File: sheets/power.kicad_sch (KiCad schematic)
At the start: 85 parts, among them Q11 C1815, Q12 A1015, Q13 A1442, T1 COIL, U11 74LS05, U12 74LS06, U28 PC4741, U29 PC4741, U33 74AS04, U37 LM2576T-5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

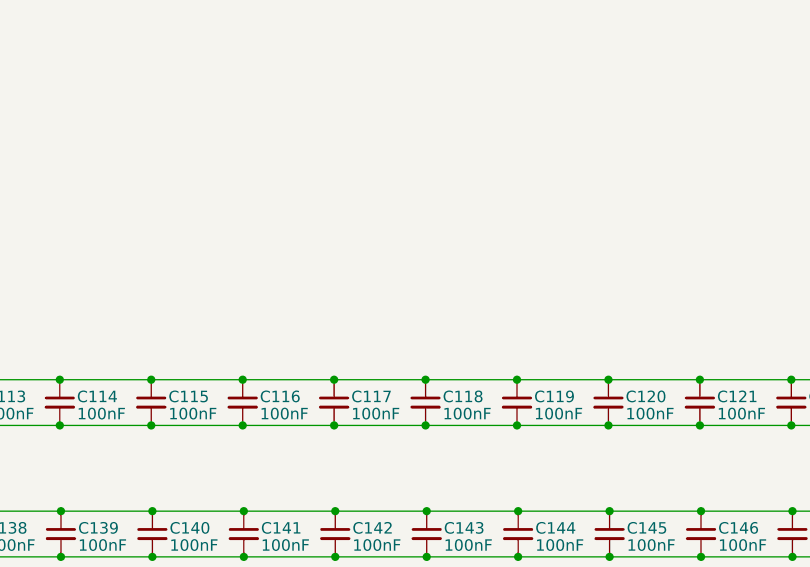
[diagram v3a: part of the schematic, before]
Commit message: Added LED
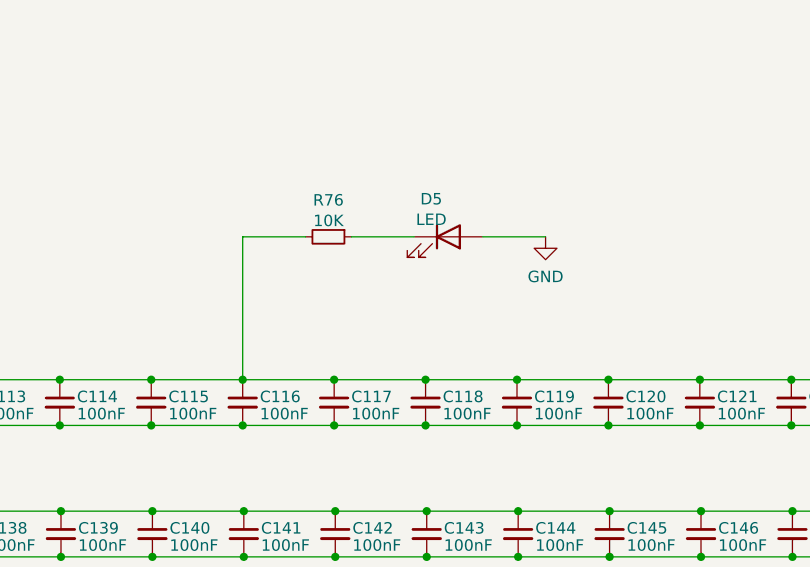
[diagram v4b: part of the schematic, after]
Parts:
- added D5: LED, 1_NeoGeoLibrary:Resistor1-5mm, symbol Device:LED
- added R76: 10K, Resistor_THT:R_Axial_DIN0309_L9.0mm_D3.2mm_P25.40mm_Horizontal, symbol Device:R_Small
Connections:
- net GND: now also D5.2 (A)
- net VCC: now also R76.2
- new net: D5.1 (K), R76.1
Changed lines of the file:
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@@
+    (stroke (width 0) (type default) (color 0 0 0 0))
+  )
+  (wire (pts (xy 197.485 111.125) (xy 204.47 111.125))
     (stroke (width 0) (type default) (color 0 0 0 0))
   )
@@
     (stroke (width 0) (type default) (color 0 0 0 0))
   )
+  (wire (pts (xy 170.815 127) (xy 170.815 111.125))
+    (stroke (width 0) (type default) (color 0 0 0 0))
+  )
   (wire (pts (xy 28.575 127) (xy 38.735 127))
     (stroke (width 0) (type default) (color 0 0 0 0))
@@
     (stroke (width 0) (type default) (color 0 0 0 0))
   )
+  (wire (pts (xy 170.815 111.125) (xy 177.8 111.125))
+    (stroke (width 0) (type default) (color 0 0 0 0))
+  )
   (wire (pts (xy 89.662 141.605) (xy 99.822 141.605))
     (stroke (width 0) (type default) (color 0 0 0 0))
@@
   )
   (wire (pts (xy 22.86 218.44) (xy 22.86 223.52))
+    (stroke (width 0) (type default) (color 0 0 0 0))
+  )
+  (wire (pts (xy 182.88 111.125) (xy 189.865 111.125))
     (stroke (width 0) (type default) (color 0 0 0 0))
   )
@@
     (pin "2")
   )
+  (symbol (lib_id "Device:R_Small") (at 180.34 111.125 270) (unit 1)
+    (in_bom yes) (on_board yes)
+    (property "Reference" "R76" (id 0) (at 180.34 107.061 90))
+    (property "Value" "10K" (id 1) (at 180.34 109.347 90))
+    (property "Footprint" "Resistor_THT:R_Axial_DIN0309_L9.0mm_D3.2mm_P25.40mm_Horizontal" (id 2) (at 180.34 111.125 0)
+      (effects (font (size 1.27 1.27)) hide)
+    )
+    (property "Datasheet" "~" (id 3) (at 180.34 111.125 0)
+      (effects (font (size 1.27 1.27)) hide)
+    )
+    (pin "1")
+    (pin "2")
+  )
   (symbol (lib_id "power:PWR_FLAG") (at 103.124 29.972 0) (unit 1)
     (in_bom yes) (on_board yes) (fields_autoplaced)
@@
     )
     (pin "1")
+  )
+  (symbol (lib_id "Device:LED") (at 193.675 111.125 0) (unit 1)
+    (in_bom yes) (on_board yes)
+    (property "Reference" "D5" (id 0) (at 191.77 106.934 0))
+    (property "Value" "LED" (id 1) (at 191.77 109.22 0))
+    (property "Footprint" "1_NeoGeoLibrary:Resistor1-5mm" (id 2) (at 193.675 111.125 0)
+      (effects (font (size 1.27 1.27)) hide)
+    )
+    (property "Datasheet" "~" (id 3) (at 193.675 111.125 0)
+      (effects (font (size 1.27 1.27)) hide)
+    )
+    (pin "1")
+    (pin "2")
   )
   (symbol (lib_id "Device:C_Small") (at 130.175 129.54 0) (unit 1)
@@
     (pin "2")
   )
+  (symbol (lib_id "power:GND") (at 204.47 111.125 0) (unit 1)
+    (in_bom yes) (on_board yes) (fields_autoplaced)
+    (property "Reference" "#PWR0281" (id 0) (at 204.47 117.475 0)
+      (effects (font (size 1.27 1.27)) hide)
+    )
+    (property "Value" "GND" (id 1) (at 204.47 115.57 0))
+    (property "Footprint" "" (id 2) (at 204.47 111.125 0)
+      (effects (font (size 1.27 1.27)) hide)
+    )
+    (property "Datasheet" "" (id 3) (at 204.47 111.125 0)
+      (effects (font (size 1.27 1.27)) hide)
+    )
+    (pin "1")
+  )
   (symbol (lib_id "74xx:74LS05") (at 123.952 259.08 0) (unit 7)

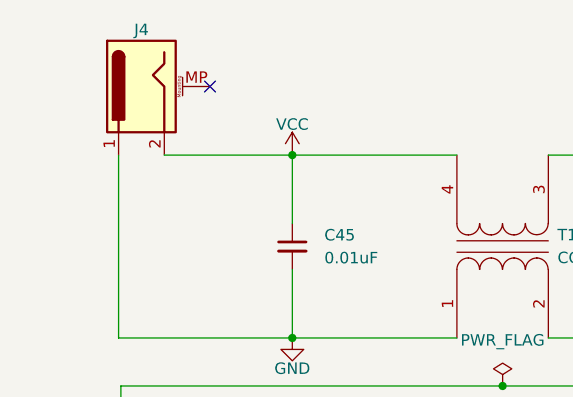
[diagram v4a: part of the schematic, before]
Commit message: Swap Barrel Jack Symbol Change Size of Resistor
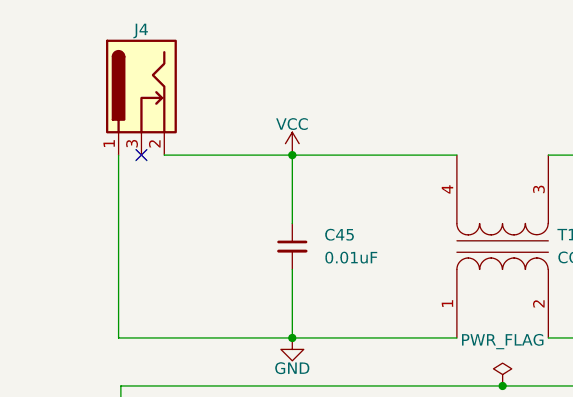
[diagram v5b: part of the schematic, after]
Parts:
- J4: symbol Connector:Barrel_Jack_MountingPin -> Connector:Barrel_Jack_Switch
- R76: footprint Resistor_THT:R_Axial_DIN0309_L9.0mm_D3.2mm_P25.40mm_Horizontal -> Resistor_THT:R_Axial_DIN0207_L6.3mm_D2.5mm_P7.62mm_Horizontal
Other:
- moved on the sheet: J4
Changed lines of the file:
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@@
   (no_connect (at 366.268 229.87))
   (no_connect (at 38.1 172.72))
-  (no_connect (at 37.338 22.352))
+  (no_connect (at 29.718 29.972))
   (no_connect (at 385.318 229.87))
   (no_connect (at 32.766 68.326))
@@
     )
   )
-  (symbol (lib_id "Connector:Barrel_Jack_MountingPin") (at 29.718 22.352 90) (mirror x) (unit 1)
+  (symbol (lib_id "Connector:Barrel_Jack_Switch") (at 29.718 22.352 90) (mirror x) (unit 1)
     (in_bom yes) (on_board yes)
     (property "Reference" "J4" (id 0) (at 29.718 16.0528 90))
@@
     (pin "1")
     (pin "2")
-    (pin "MP")
+    (pin "3")
   )
   (symbol (lib_id "power:PWR_FLAG") (at 256.413 65.786 0) (unit 1)
@@
     (property "Reference" "R76" (id 0) (at 180.34 107.061 90))
     (property "Value" "10K" (id 1) (at 180.34 109.347 90))
-    (property "Footprint" "Resistor_THT:R_Axial_DIN0309_L9.0mm_D3.2mm_P25.40mm_Horizontal" (id 2) (at 180.34 111.125 0)
-      (effects (font (size 1.27 1.27)) hide)
-    )
+    (property "Footprint" "Resistor_THT:R_Axial_DIN0207_L6.3mm_D2.5mm_P7.62mm_Horizontal" (id 2) (at 180.34 111.125 0)
+      (effects (font (size 1.27 1.27)) hide)
+    )

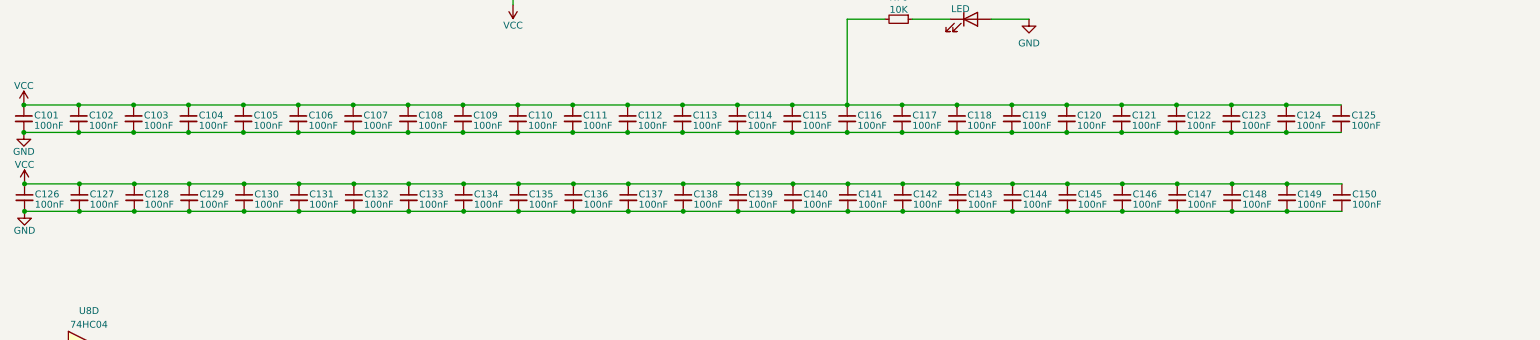
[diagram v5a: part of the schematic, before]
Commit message: Remove Spare Caps
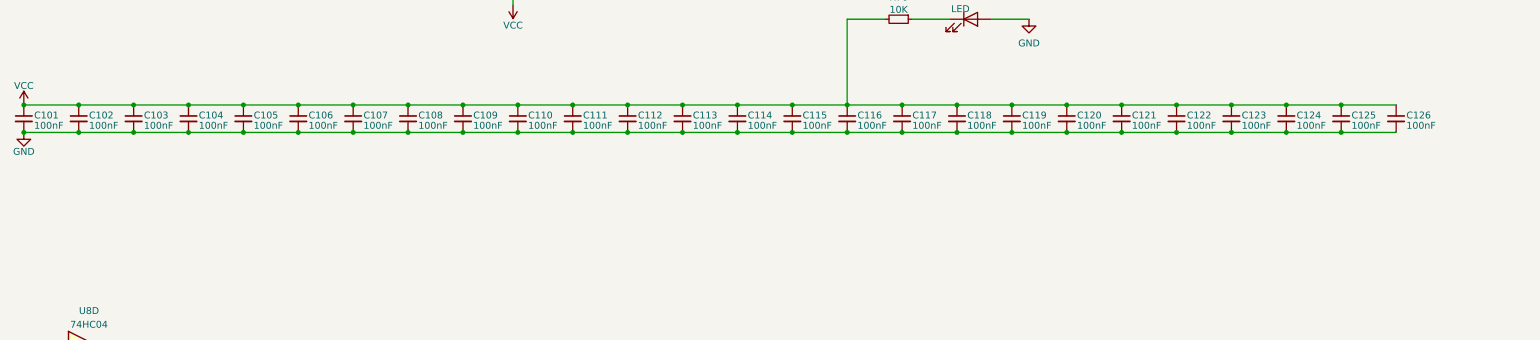
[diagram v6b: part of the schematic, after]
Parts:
- removed C127, C128, C129, C130, C131, C132, C133, C134, C135, C136, C137, C138, C139, C140, C141, C142, C143, C144, C145, C146, C147, C148, C149, C150: 100nF, 1_NeoGeoLibrary:CAP3-5mm, symbol Device:C_Small
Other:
- moved on the sheet: C126

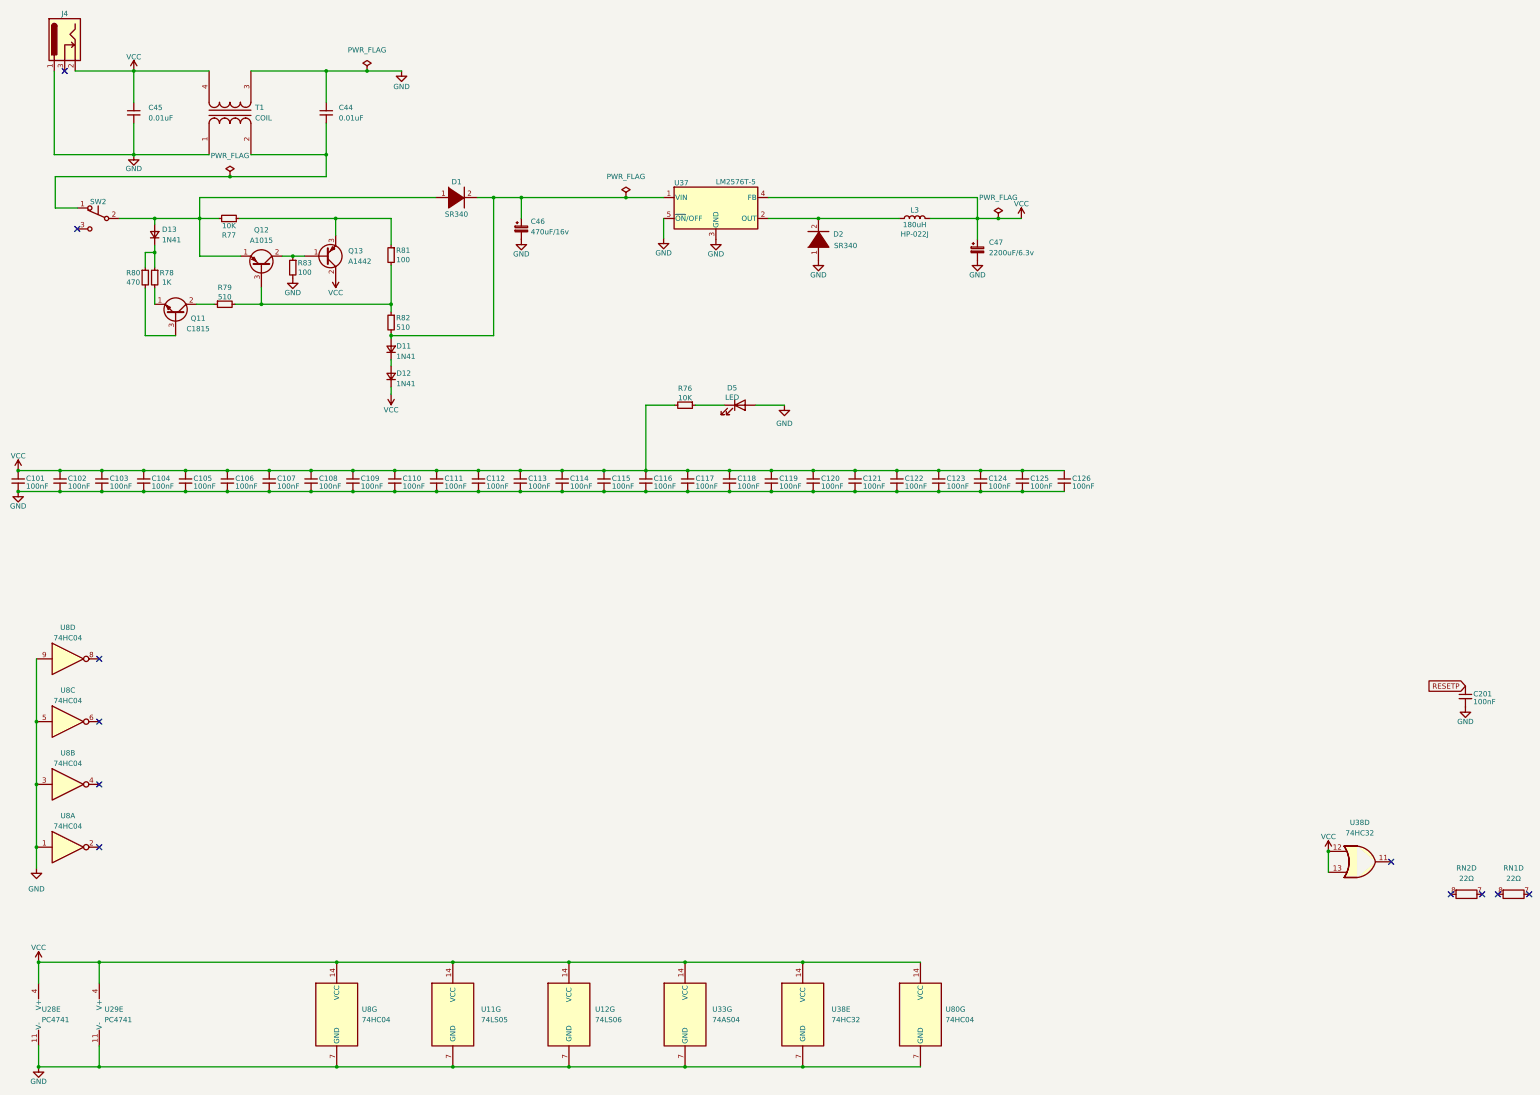
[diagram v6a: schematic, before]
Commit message: Upgrade Schematics to Kicad 7.0
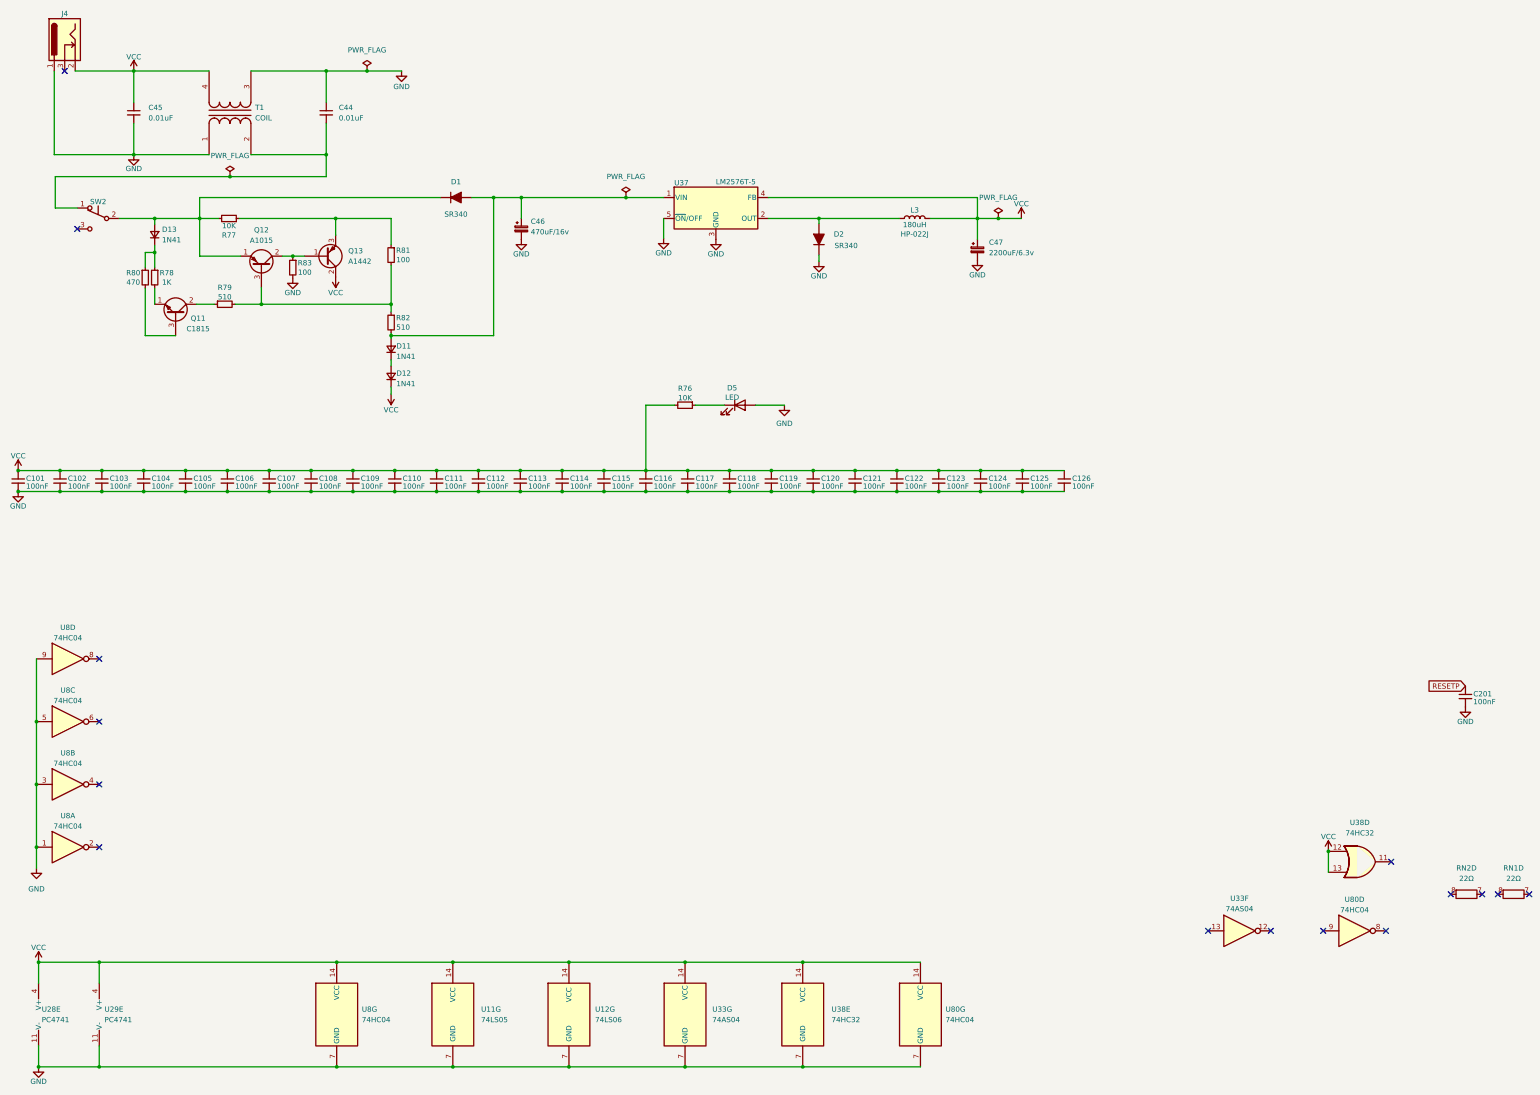
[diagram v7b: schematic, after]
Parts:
- added unit 6 of U33
- added unit 4 of U80
- D1, D2: symbol pspice:DIODE -> Device:D_Filled
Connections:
- no-connect marks 11 -> 15
